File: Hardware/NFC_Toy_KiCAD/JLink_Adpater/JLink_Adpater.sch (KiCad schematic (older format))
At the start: 2 parts, among them J1 JLink_Mini, J2 JLink_Mini

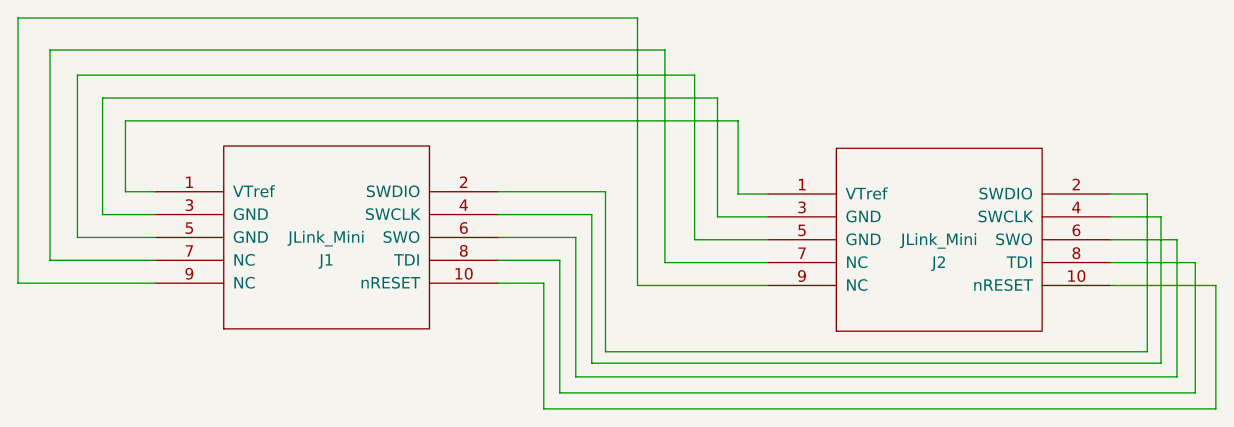
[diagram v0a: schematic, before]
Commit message: Added inverted JLink adapter. First working code.
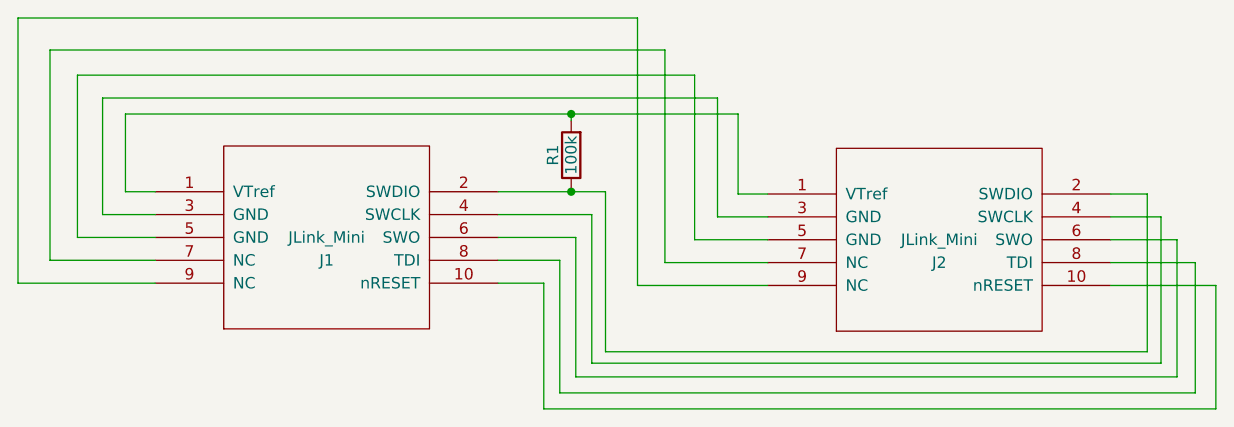
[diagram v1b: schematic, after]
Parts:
- added R1: 100k, Resistors_SMD:R_0603_HandSoldering, symbol R
- J1: footprint Socket_Strips:Socket_Strip_Straight_2x05_Pitch1.27mm -> NFC_Toy_Lib:JLink_Mini_0p05_inverted
- J2: footprint Socket_Strips:Socket_Strip_Straight_2x05_Pitch2.54mm -> NFC_Toy_Lib:J-Link_0p1in_inverted
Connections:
- net at J1.1 (VTref), J2.1 (VTref): now also R1.2
- net at J1.2 (SWDIO), J2.2 (SWDIO): now also R1.1
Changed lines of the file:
@@
 LIBS:valves
 LIBS:JLink_Mini
+LIBS:JLink_Adpater-cache
 EELAYER 25 0
 EELAYER END
@@
 F 0 "J1" H 4410 3640 50  0000 C CNN
 F 1 "JLink_Mini" H 4410 3740 50  0000 C CNN
-F 2 "Socket_Strips:Socket_Strip_Straight_2x05_Pitch1.27mm" H 4410 3740 50  0001 C CNN
+F 2 "NFC_Toy_Lib:JLink_Mini_0p05_inverted" H 4410 3740 50  0001 C CNN
 F 3 "DOCUMENTATION" H 4410 3740 50  0001 C CNN
 	1    4410 3740
@@
 F 0 "J2" H 7090 3650 50  0000 C CNN
 F 1 "JLink_Mini" H 7090 3750 50  0000 C CNN
-F 2 "Socket_Strips:Socket_Strip_Straight_2x05_Pitch2.54mm" H 7090 3750 50  0001 C CNN
+F 2 "NFC_Toy_Lib:J-Link_0p1in_inverted" H 7090 3750 50  0001 C CNN
 F 3 "DOCUMENTATION" H 7090 3750 50  0001 C CNN
 	1    7090 3750
@@
 $EndComp
 Wire Wire Line
-	3530 3230 6210 3230
+	3530 3200 6210 3200
 Wire Wire Line
-	6210 3230 6210 3550
+	6210 3200 6210 3550
 Wire Wire Line
 	6210 3550 6340 3550
 Wire Wire Line
-	3530 3230 3530 3540
+	3530 3200 3530 3540
 Wire Wire Line
 	3530 3540 3660 3540
@@
 Wire Wire Line
 	8300 3950 7840 3950
+$Comp
+L R R1
+U 1 1 5B0010A4
+P 5480 3380
+F 0 "R1" V 5560 3380 50  0000 C CNN
+F 1 "100k" V 5480 3380 50  0000 C CNN
+F 2 "Resistors_SMD:R_0603_HandSoldering" V 5410 3380 50  0001 C CNN
+F 3 "" H 5480 3380 50  0001 C CNN
+	1    5480 3380
+	-1   0    0    1
+$EndComp
+Wire Wire Line
+	5480 3530 5480 3540
+Connection ~ 5480 3540
+Wire Wire Line
+	5480 3230 5480 3200
+Connection ~ 5480 3200
 $EndSCHEMATC
